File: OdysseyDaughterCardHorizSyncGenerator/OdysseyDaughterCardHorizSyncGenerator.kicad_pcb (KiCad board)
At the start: 2 copper layers, 34.4 x 46.6 mm, 16 parts, among them Q1 BC547B, Q2 BC556B, Q3 2N3904, X1 OdysseyDaughterCard

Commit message: OdysseyDaughterCardHorizSyncGenerator: Open and close in KiCad 6, fix symbol library paths
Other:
- net class Default removed

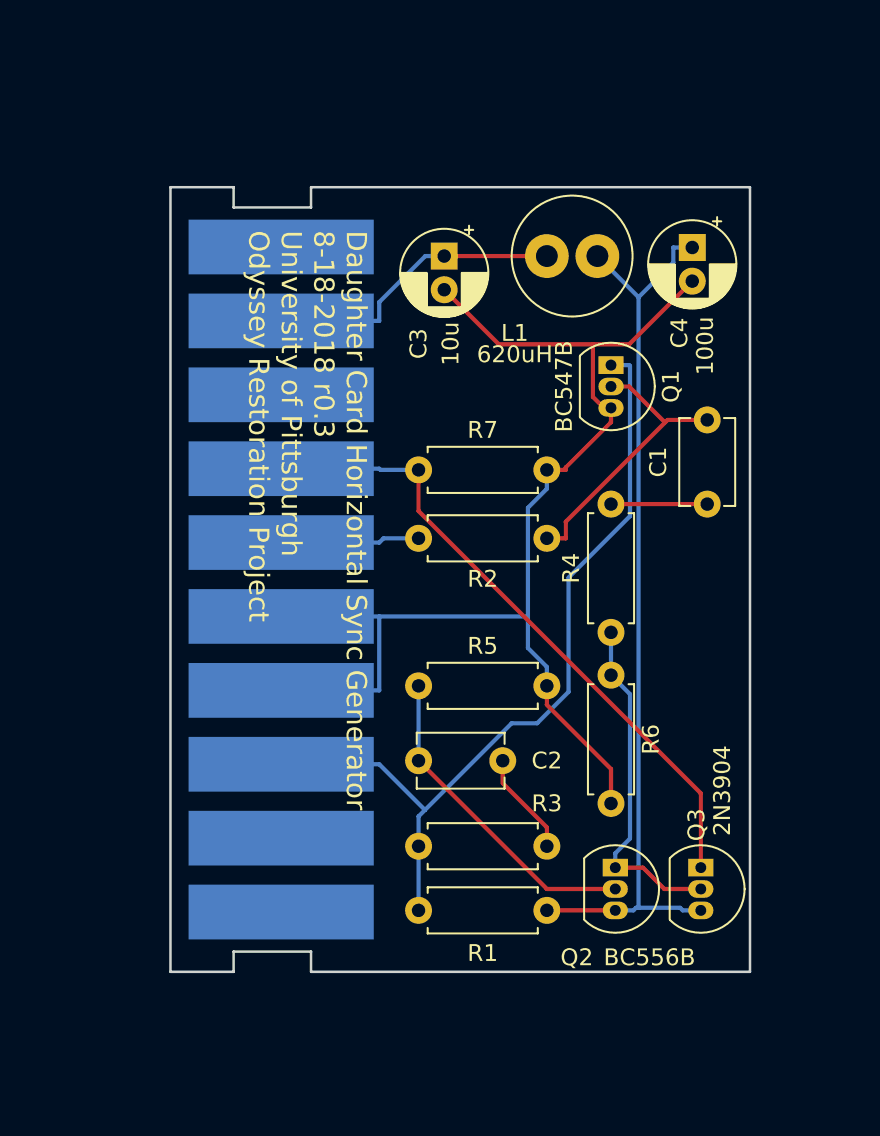
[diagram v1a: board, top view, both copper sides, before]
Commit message: OdysseyDaughterCardHorizSyncGenerator wider transistor footprint, add logo, generate pdf, images, 3d models
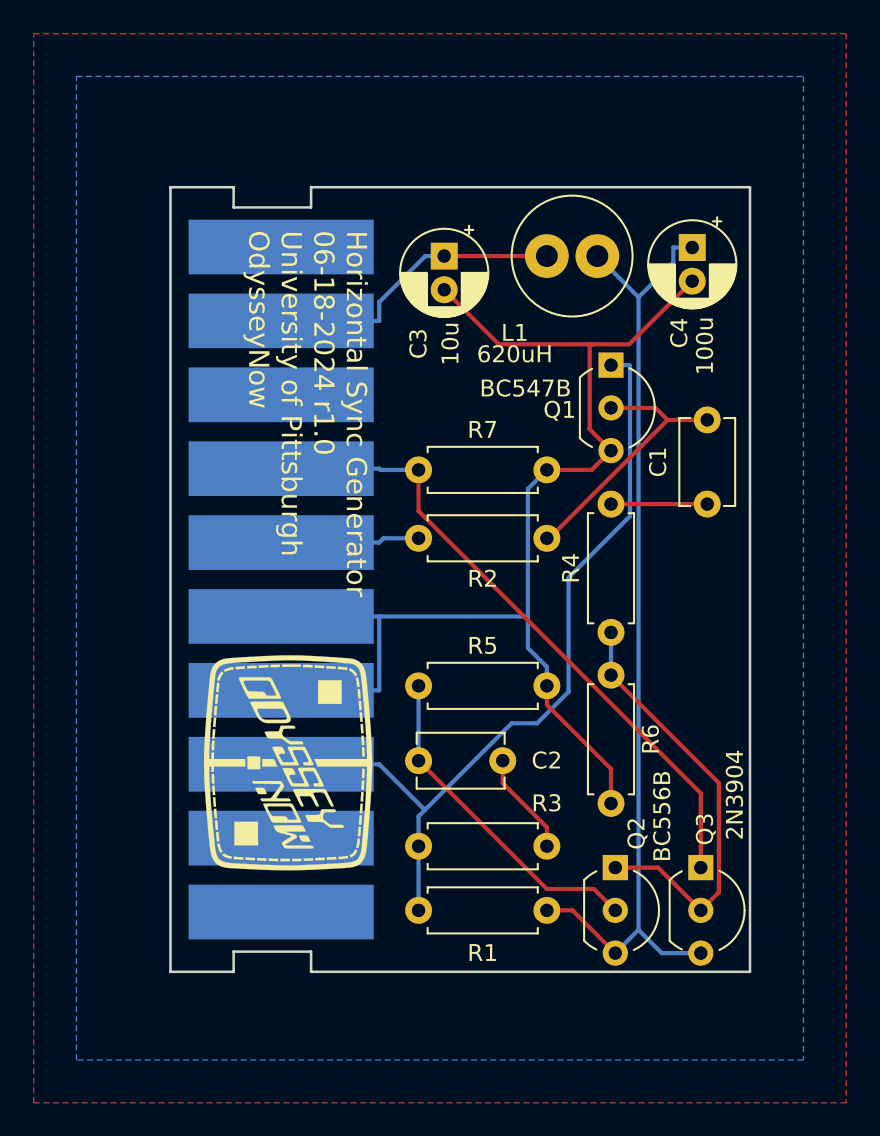
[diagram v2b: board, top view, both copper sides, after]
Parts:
- added X1: OdysseyNow_Logo, Odyssey_Daughter_Card:OdysseyNowLogo, F.Cu at (130.2, 111.6)
- Q1, Q2, Q3: footprint Package_TO_SOT_THT:TO-92_Inline -> Package_TO_SOT_THT:TO-92_Inline_Wide
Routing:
- net Net-(Q2-C): track 20.4 -> 25.7 mm
- net Net-(Q2-E): track 53.9 -> 57.3 mm
- net GND: track 75.4 -> 76.1 mm
- net Net-(Q1-B): track 17.1 -> 16.5 mm
- net Net-(Q2-B): track 19.3 -> 19.8 mm
- added copper zone on F.Cu, net /Card9
- added copper zone on B.Cu, net GND
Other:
- board text added: "Horizontal Sync Generator 06-18-2024 r1.0 University of Pittsburgh OdysseyNow"
- board text removed: "Daughter Card Horizontal Sync Generator 8-18-2018 r0.3 University of Pittsburgh Odyssey Restoration Project"
